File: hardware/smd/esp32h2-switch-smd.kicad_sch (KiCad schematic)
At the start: 4 parts, among them J1 Screw_Terminal_01x02, J2 Screw_Terminal_01x02

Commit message: Drop all tht legacy footprints
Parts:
- J1, J2: footprint TerminalBlock_Phoenix:TerminalBlock_Phoenix_MKDS-1,5-2-5.08_1x02_P5.08mm_Horizontal -> (none)
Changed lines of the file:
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@@
 			)
 		)
-		(property "Footprint" "TerminalBlock_Phoenix:TerminalBlock_Phoenix_MKDS-1,5-2-5.08_1x02_P5.08mm_Horizontal"
+		(property "Footprint" ""
 			(at 196.85 88.9 0)
 			(effects
@@
 			)
 		)
-		(property "Footprint" "TerminalBlock_Phoenix:TerminalBlock_Phoenix_MKDS-1,5-2-5.08_1x02_P5.08mm_Horizontal"
+		(property "Footprint" ""
 			(at 95.25 87.63 0)
 			(effects

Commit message: Assign footprints and JLC numbers (plus minor changes)
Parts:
- J1, J2: footprint (none) -> TerminalBlock_Phoenix:TerminalBlock_Phoenix_PT-1,5-2-5.0-H_1x02_P5.00mm_Horizontal; JLCPCB (none) -> C5188438

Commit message: Complete PCB and schematics after fucking a lot of iterations
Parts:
- NT1, NT2: footprint (none) -> KiCadX_NetTies:NetTie_2_D0.5_P4.0
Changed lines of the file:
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@@
 			)
 		)
-		(property "Footprint" ""
+		(property "Footprint" "KiCadX_NetTies:NetTie_2_D0.5_P4.0"
 			(at 110.49 91.44 0)
 			(effects
@@
 			)
 		)
-		(property "Footprint" ""
+		(property "Footprint" "KiCadX_NetTies:NetTie_2_D0.5_P4.0"
 			(at 110.49 87.63 0)
 			(effects

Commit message: Rename JLCPCB property to LCSC PN across schematic files
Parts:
- J1, J2: JLCPCB C5188438 -> (none); LCSC PN (none) -> C5188438
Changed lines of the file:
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@@
 			)
 		)
-		(property "JLCPCB" "C5188438"
+		(property "LCSC PN" "C5188438"
 			(at 196.85 88.9 0)
 			(effects
@@
 			)
 		)
-		(property "JLCPCB" "C5188438"
+		(property "LCSC PN" "C5188438"
 			(at 95.25 87.63 0)
 			(effects

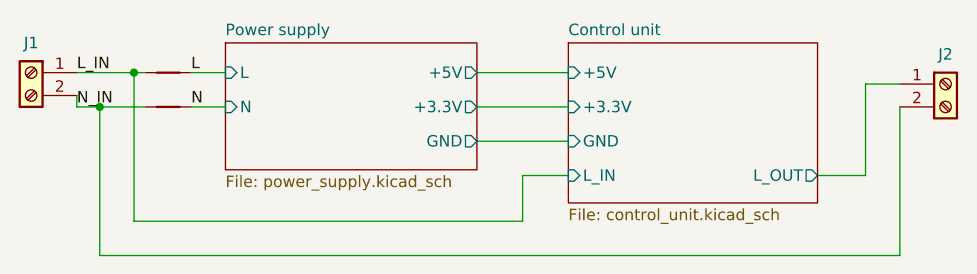
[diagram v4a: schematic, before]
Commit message: Relink symbols and footprints to new lib and fix few errors
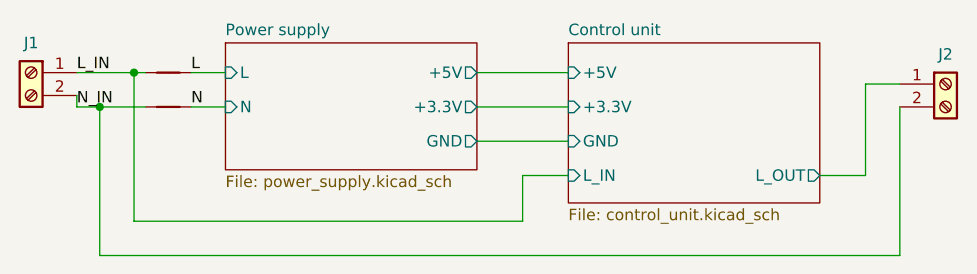
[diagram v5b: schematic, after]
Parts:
- NT1, NT2: footprint KiCadX_NetTies:NetTie_2_D0.5_P4.0 -> PCM_SKC_NetTies:NetTie_2_D0.5_P4.0
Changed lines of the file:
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@@
+	(wire
+		(pts
+			(xy 144.78 87.63) (xy 154.94 87.63)
+		)
+		(stroke
+			(width 0)
+			(type default)
+		)
+	)
 	(wire
 		(pts
@@
 	(wire
 		(pts
+			(xy 182.88 99.06) (xy 187.96 99.06)
+		)
+		(stroke
+			(width 0)
+			(type default)
+		)
+	)
+	(wire
+		(pts
 			(xy 100.33 91.44) (xy 102.87 91.44)
 		)
@@
 	(wire
 		(pts
-			(xy 182.626 99.06) (xy 187.96 99.06)
-		)
-		(stroke
-			(width 0)
-			(type default)
-		)
-	)
-	(wire
-		(pts
 			(xy 113.03 91.44) (xy 116.84 91.44)
 		)
@@
 		(pts
 			(xy 106.68 87.63) (xy 106.68 104.14)
-		)
-		(stroke
-			(width 0)
-			(type default)
-		)
-	)
-	(wire
-		(pts
-			(xy 144.78 87.63) (xy 154.94 87.63)
 		)
 		(stroke
@@
 			)
 		)
-		(property "Footprint" "KiCadX_NetTies:NetTie_2_D0.5_P4.0"
+		(property "Footprint" "PCM_SKC_NetTies:NetTie_2_D0.5_P4.0"
 			(at 110.49 91.44 0)
 			(effects
@@
 			)
 		)
-		(property "Footprint" "KiCadX_NetTies:NetTie_2_D0.5_P4.0"
+		(property "Footprint" "PCM_SKC_NetTies:NetTie_2_D0.5_P4.0"
 			(at 110.49 87.63 0)
 			(effects
@@
 	(sheet
 		(at 154.94 84.328)
-		(size 27.686 17.78)
+		(size 27.94 17.78)
 		(exclude_from_sim no)
 		(in_bom yes)
@@
 		)
 		(pin "L_OUT" output
-			(at 182.626 99.06 0)
-			(effects
-				(font
+			(at 182.88 99.06 0)
+			(effects
+				(font
